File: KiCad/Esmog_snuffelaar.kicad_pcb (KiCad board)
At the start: 2 copper layers, 135 x 66.5 mm, 277 parts, among them J1 Conn_01x03, J10 AudioJack, J2 Conn_01x03, J3 Conn_01x10_Pin, J4 Conn_01x10_Pin, J5 Conn_01x10_Pin, J6 Conn_01x10_Pin, J7 Conn_01x10_Pin, J9 Conn_Coaxial, P1 USB_C_Plug_USB2.0, Q1 2N7002, Q10 2N7002, Q11 2N7002, Q2 2N7002, Q3 BSR17A, Q4 BC547B, Q5 BC547B, Q6 2N7002, Q7 2N7002, Q8 2N7002, Q9 2N7002, SW1 SW_Push, SW2 SW_Push, SW3 SW_Push, U1 TPS62056DGS, U10 74HC590, U11 4017, U2 TPS62056DGS, U3 LM66100DCK, U4 LM66100DCK, U5 STM32L476RGT6, U6 CP2102N-Axx-xQFN24, U7 TJM4558CDT, U8 74HC590, U9 74HC590, Y1 Crystal_GND24

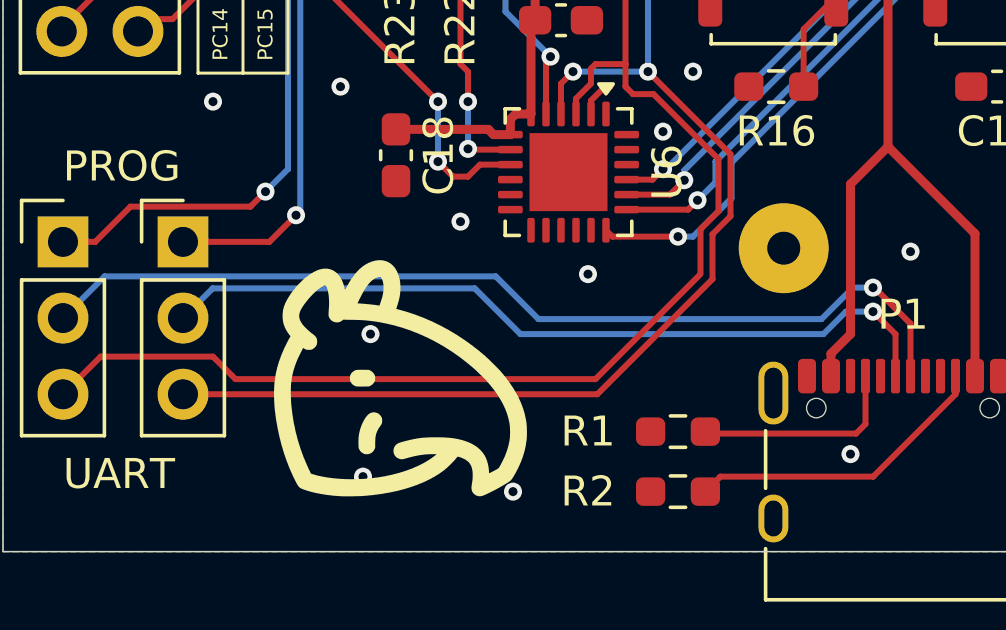
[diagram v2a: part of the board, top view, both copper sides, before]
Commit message: d+ and d- length matching
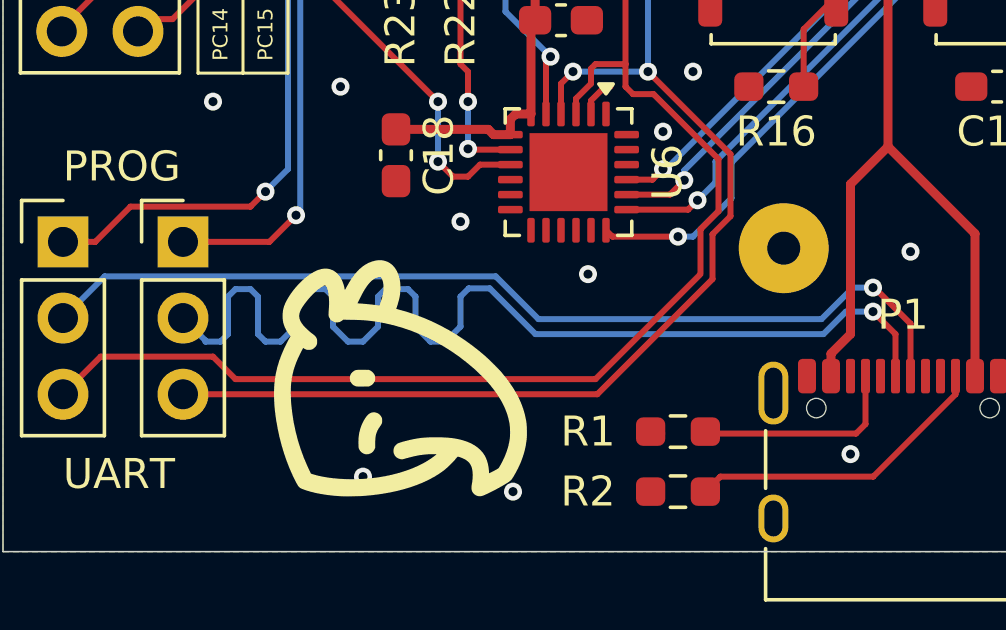
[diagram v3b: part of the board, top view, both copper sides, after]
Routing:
- net Net-(J2-Pin_2): track 26.8 -> 36.2 mm
- net GND: vias 106 -> 105
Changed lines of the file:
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@@
 	)
 	(via
-		(at 106.75 83.25)
-		(size 0.6)
-		(drill 0.3)
-		(layers "F.Cu" "B.Cu")
-		(free yes)
-		(net "GND")
-	)
-	(via
 		(at 166.25 77.5)
 		(size 0.6)
@@
 	)
 	(segment
-		(start 101.49 81.725)
-		(end 100.5 82.715)
+		(start 104.5 81.75)
+		(end 104.25 82)
+		(width 0.2)
+		(layer "B.Cu")
+		(net "Net-(J2-Pin_2)")
+	)
+	(segment
+		(start 103.25 83.5)
+		(end 103 83.25)
+		(width 0.2)
+		(layer "B.Cu")
+		(net "Net-(J2-Pin_2)")
+	)
+	(segment
+		(start 104.25 83)
+		(end 103.75 83.5)
+		(width 0.2)
+		(layer "B.Cu")
+		(net "Net-(J2-Pin_2)")
+	)
+	(segment
+		(start 102 83.25)
+		(end 101.75 83.5)
+		(width 0.2)
+		(layer "B.Cu")
+		(net "Net-(J2-Pin_2)")
+	)
+	(segment
+		(start 103.75 83.5)
+		(end 103.25 83.5)
+		(width 0.2)
+		(layer "B.Cu")
+		(net "Net-(J2-Pin_2)")
+	)
+	(segment
+		(start 109.75 82)
+		(end 109.75 83)
+		(width 0.2)
+		(layer "B.Cu")
+		(net "Net-(J2-Pin_2)")
+	)
+	(segment
+		(start 107.25 81.75)
+		(end 107 82)
+		(width 0.2)
+		(layer "B.Cu")
+		(net "Net-(J2-Pin_2)")
+	)
+	(segment
+		(start 105.5 82)
+		(end 105.25 81.75)
 		(width 0.2)
 		(layer "B.Cu")
@@
 	)
 	(segment
+		(start 122.598528 82.5)
+		(end 121.848528 83.25)
+		(width 0.2)
+		(layer "B.Cu")
+		(net "Net-(J2-Pin_2)")
+	)
+	(segment
+		(start 112.25 83.25)
+		(end 110.725 81.725)
+		(width 0.2)
+		(layer "B.Cu")
+		(net "Net-(J2-Pin_2)")
+	)
+	(segment
+		(start 109.75 83)
+		(end 109.25 83.5)
+		(width 0.2)
+		(layer "B.Cu")
+		(net "Net-(J2-Pin_2)")
+	)
+	(segment
+		(start 106 83.5)
+		(end 105.5 83)
+		(width 0.2)
+		(layer "B.Cu")
+		(net "Net-(J2-Pin_2)")
+	)
+	(segment
+		(start 102 82)
+		(end 102 83.25)
+		(width 0.2)
+		(layer "B.Cu")
+		(net "Net-(J2-Pin_2)")
+	)
+	(segment
+		(start 102.25 81.75)
+		(end 102 82)
+		(width 0.2)
+		(layer "B.Cu")
+		(net "Net-(J2-Pin_2)")
+	)
+	(segment
+		(start 109.25 83.5)
+		(end 108.75 83.5)
+		(width 0.2)
+		(layer "B.Cu")
+		(net "Net-(J2-Pin_2)")
+	)
+	(segment
+		(start 108.25 83)
+		(end 108.25 82)
+		(width 0.2)
+		(layer "B.Cu")
+		(net "Net-(J2-Pin_2)")
+	)
+	(segment
+		(start 101.25 83.465)
+		(end 100.5 82.715)
+		(width 0.2)
+		(layer "B.Cu")
+		(net "Net-(J2-Pin_2)")
+	)
+	(segment
+		(start 104.25 82)
+		(end 104.25 83)
+		(width 0.2)
+		(layer "B.Cu")
+		(net "Net-(J2-Pin_2)")
+	)
+	(segment
+		(start 108.25 82)
+		(end 108 81.75)
+		(width 0.2)
+		(layer "B.Cu")
+		(net "Net-(J2-Pin_2)")
+	)
+	(segment
+		(start 103 83.25)
+		(end 103 82)
+		(width 0.2)
+		(layer "B.Cu")
+		(net "Net-(J2-Pin_2)")
+	)
+	(segment
+		(start 105.5 83)
+		(end 105.5 82)
+		(width 0.2)
+		(layer "B.Cu")
+		(net "Net-(J2-Pin_2)")
+	)
+	(segment
+		(start 110.725 81.725)
+		(end 110.025 81.725)
+		(width 0.2)
+		(layer "B.Cu")
+		(net "Net-(J2-Pin_2)")
+	)
+	(segment
+		(start 106.5 83.5)
+		(end 106 83.5)
+		(width 0.2)
+		(layer "B.Cu")
+		(net "Net-(J2-Pin_2)")
+	)
+	(segment
+		(start 103 82)
+		(end 102.75 81.75)
+		(width 0.2)
+		(layer "B.Cu")
+		(net "Net-(J2-Pin_2)")
+	)
+	(segment
+		(start 108.75 83.5)
+		(end 108.25 83)
+		(width 0.2)
+		(layer "B.Cu")
+		(net "Net-(J2-Pin_2)")
+	)
+	(segment
+		(start 101.25 83.5)
+		(end 101.25 83.465)
+		(width 0.2)
+		(layer "B.Cu")
+		(net "Net-(J2-Pin_2)")
+	)
+	(segment
+		(start 108 81.75)
+		(end 107.25 81.75)
+		(width 0.2)
+		(layer "B.Cu")
+		(net "Net-(J2-Pin_2)")
+	)
+	(segment
+		(start 105.25 81.75)
+		(end 104.5 81.75)
+		(width 0.2)
+		(layer "B.Cu")
+		(net "Net-(J2-Pin_2)")
+	)
+	(segment
+		(start 110.025 81.725)
+		(end 109.75 82)
+		(width 0.2)
+		(layer "B.Cu")
+		(net "Net-(J2-Pin_2)")
+	)
+	(segment
 		(start 121.848528 83.25)
-		(end 111.75 83.25)
+		(end 112.25 83.25)
 		(width 0.2)
 		(layer "B.Cu")
@@
 	)
 	(segment
-		(start 122.598528 82.5)
-		(end 121.848528 83.25)
+		(start 101.75 83.5)
+		(end 101.25 83.5)
+		(width 0.2)
+		(layer "B.Cu")
+		(net "Net-(J2-Pin_2)")
+	)
+	(segment
+		(start 107 82)
+		(end 107 83)
 		(width 0.2)
 		(layer "B.Cu")
@@
 	)
 	(segment
-		(start 110.225 81.725)
-		(end 101.49 81.725)
+		(start 102.75 81.75)
+		(end 102.25 81.75)
 		(width 0.2)
 		(layer "B.Cu")
@@
 	)
 	(segment
-		(start 111.75 83.25)
-		(end 110.225 81.725)
+		(start 107 83)
+		(end 106.5 83.5)
 		(width 0.2)
 		(layer "B.Cu")
